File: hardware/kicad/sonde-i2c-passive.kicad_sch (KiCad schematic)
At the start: 9 parts, among them J1 Vers BA J1/J2 (WR-MPC3 2x2, p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, J2 Vers analyseur logique FX2, U1 74LVC2G17

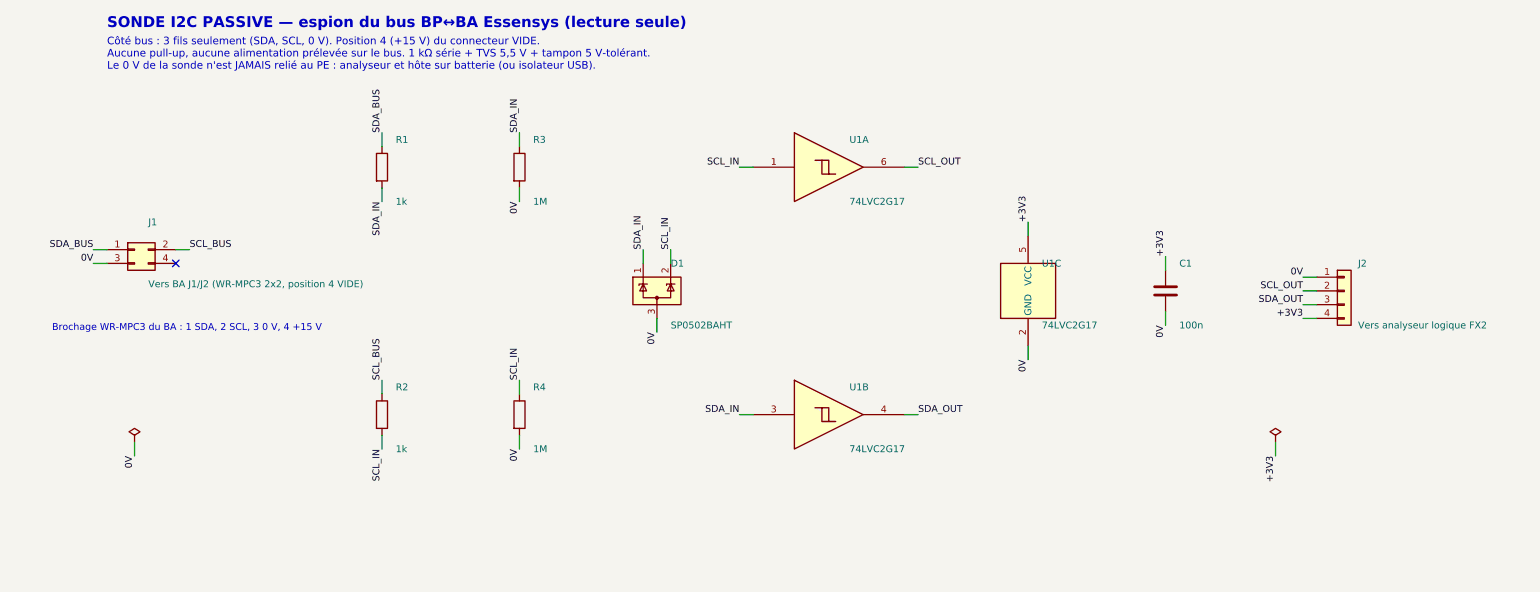
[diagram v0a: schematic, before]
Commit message: fix(hardware): schémas de la sonde corrigés après relecture critique (essensys-hub/essensys-i2c-ba-sniffer#5)
KiCad :
- schéma câblé de gauche à droite (SCL en haut, SDA en bas) au lieu d'étiquettes
  partout ; symboles 0 V / +3V3 locaux ; J1 sans empreinte trompeuse (câble) ;
- J2 réordonné : 1 +3,3 V, 2 SCL (D0), 3 SDA (D1), 4 0 V (pas de croisement) ;
- check_netlist.py : la netlist exportée doit correspondre au circuit voulu
  (lancé en CI après l'ERC) ; export PNG recadré sur le contenu.

Fritzing (deux croquis, pièces embarquées dessinées par le générateur) :
- implantation sur plaque à pastilles : repères et valeurs lisibles, vrai
  connecteur 2x2 avec la position 4 (+15 V) barrée, fils à angle droit, bus 0 V
  en anneau, jonctions soudées marquées, deux croisements isolés signalés ;
- ensemble : BA, câble, sonde, analyseur FX2 (voies étiquetées), Raspberry Pi
  sur batterie, câble USB, masse commune (GND de l'analyseur et broche 9),
  Ethernet barré, zone « même 0 V que l'armoire ».

Feature: i2c-ba-sniffer-2026-10-009

Co-Authored-By: Claude Opus 5.5 <noreply@anthropic.com>
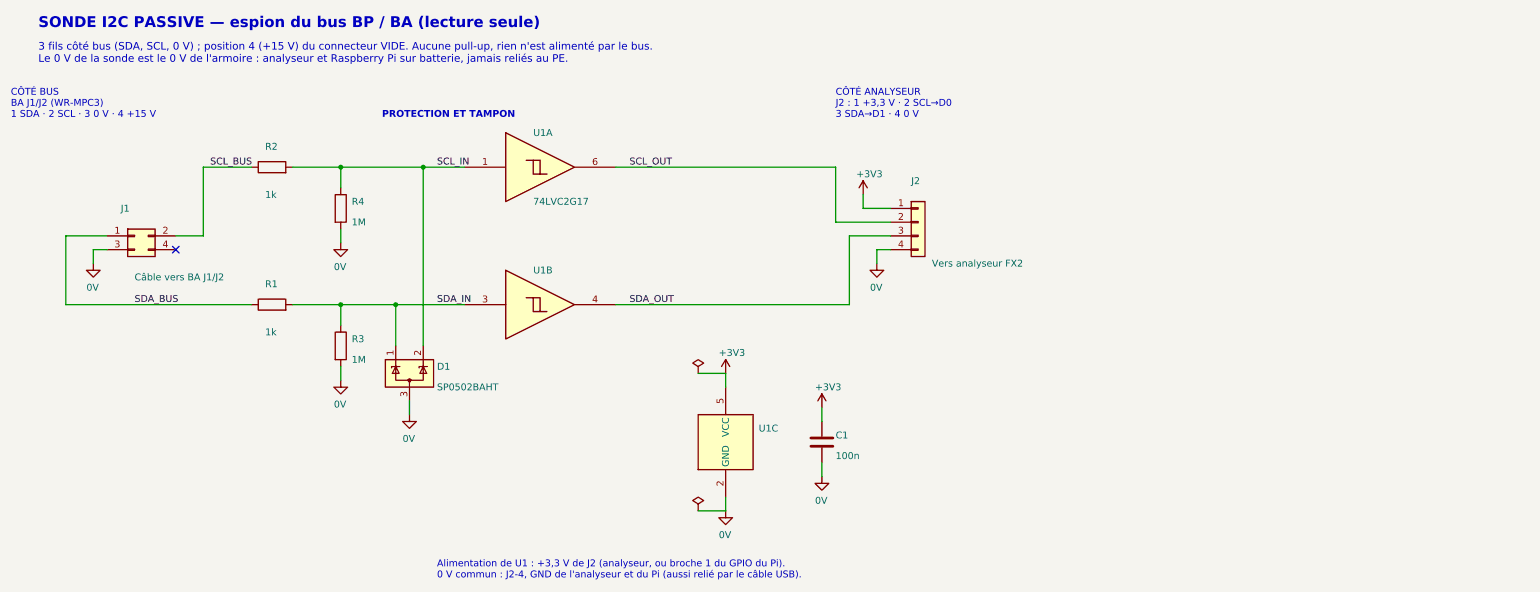
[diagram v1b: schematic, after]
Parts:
- D1: Note TVS 2 voies, sur adaptateur SOT-23 vers DIP -> Sur adaptateur SOT-23 vers SIP3
- J1: value Vers BA J1/J2 (WR-MPC3 2x2, position 4 VIDE) -> Câble vers BA J1/J2; footprint Connector_Molex:Molex_Micro-Fit_3.0_43045-0412_2x02_P3.00mm_Vertical -> (none); MPN WR-MPC3 2x2 boîtier femelle câble (à confirmer, tâche 5.1) -> WR-MPC3 2x2, boîtier femelle câble (à confirmer, tâche 5.1); Note Seuls les contacts 1, 2, 3 sont sertis ; la position 4 (+15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 -> Boîtier câble ; seuls les contacts 1, 2, 3 sont sertis, la 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
- J2: value Vers analyseur logique FX2 -> Vers analyseur FX2; Note 1 GND, 2 voie D0 (SCL), 3 voie D1 (SDA), 4 +3,3 V de l'anal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 -> 1 +3,3 V, 2 SCL vers D0, 3 SDA vers D1, 4 0 V (GND de l'ana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
- R1: Note Résistance série : limite le courant en cas d'erreur -> Série SDA
- R2: Note Résistance série : limite le courant en cas d'erreur -> Série SCL
- R3: Note Rappel au 0 V si la sonde est débranchée (5 µA sous 5 V, né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 -> Rappel SDA au 0 V
- R4: Note Rappel au 0 V si la sonde est débranchée -> Rappel SCL au 0 V
- U1: Note Entrées tolérantes 5,5 V sous VCC = 3,3 V ; sur adaptateur 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 -> Entrées tolérantes 5,5 V (Ioff) sous VCC = 3,3 V ; sur adap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
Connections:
- net +3V3: now also J2.1 (Pin_1); no longer J2.4 (Pin_4)
- net 0V: now also J2.4 (Pin_4); no longer J2.1 (Pin_1)
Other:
- note added: "3 fils côté bus (SDA, SCL, 0 V) ; position 4 (+15 V) du connecteur VIDE. Aucune pull-up, rien n'est alimenté par le bus. Le 0 V de la sonde est le 0 V de l'armoire : analyseur et Raspberry Pi sur batterie, jamais reliés au PE."
- note added: "Alimentation de U1 : +3,3 V de J2 (analyseur, ou broche 1 du GPIO du Pi). 0 V commun : J2-4, GND de l'analyseur et du Pi (aussi relié par le câble USB)."
- note added: "CÔTÉ ANALYSEUR J2 : 1 +3,3 V · 2 SCL→D0 3 SDA→D1 · 4 0 V"
- note added: "CÔTÉ BUS BA J1/J2 (WR-MPC3) 1 SDA · 2 SCL · 3 0 V · 4 +15 V"
- note added: "PROTECTION ET TAMPON"
- note added: "SONDE I2C PASSIVE — espion du bus BP / BA (lecture seule)"
- note removed: "Brochage WR-MPC3 du BA : 1 SDA, 2 SCL, 3 0 V, 4 +15 V"
- note removed: "Côté bus : 3 fils seulement (SDA, SCL, 0 V). Position 4 (+15 V) du connecteur VIDE. Aucune pull-up, aucune alimentation prélevée sur le bus. 1 kΩ série + TVS 5,5 V + tampon 5 V-tolérant. Le 0 V de la sonde n'est JAMAIS relié au PE : analyseur et hôte sur batterie (ou isolateur USB)."
- note removed: "SONDE I2C PASSIVE — espion du bus BP↔BA Essensys (lecture seule)"
- moved on the sheet: C1, D1, J1, J2, R1, R2, R3, R4, U1A, U1B, U1C
